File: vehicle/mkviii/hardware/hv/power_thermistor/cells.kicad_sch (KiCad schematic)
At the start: 53 parts, among them J10 Battery Cell Spot Weld, J11 Battery Cell Spot Weld, J12 Battery Cell Spot Weld, J13 Battery Cell Spot Weld, J14 Battery Cell Spot Weld, J15 Battery Cell Spot Weld, J16 Battery Cell Spot Weld, J17 Battery Cell Spot Weld, J18 Battery Cell Spot Weld, J19 Battery Cell Spot Weld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

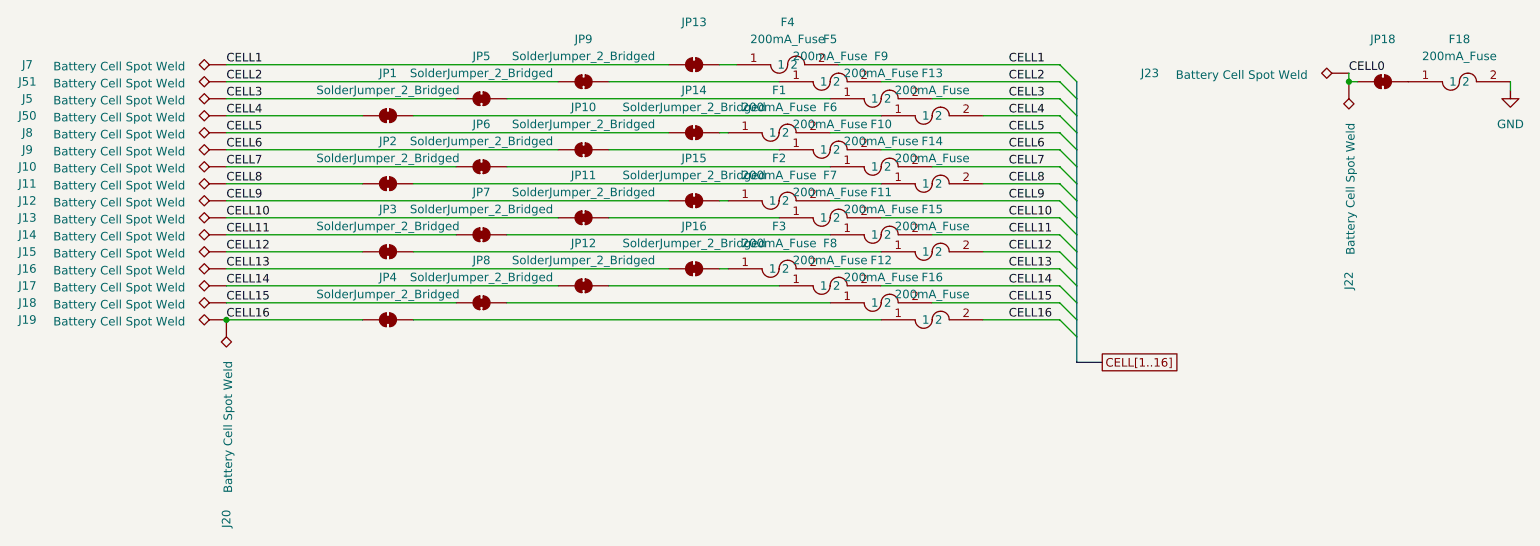
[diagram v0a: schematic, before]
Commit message: Minor redcube schematic changes; added some silkscreen; added production files
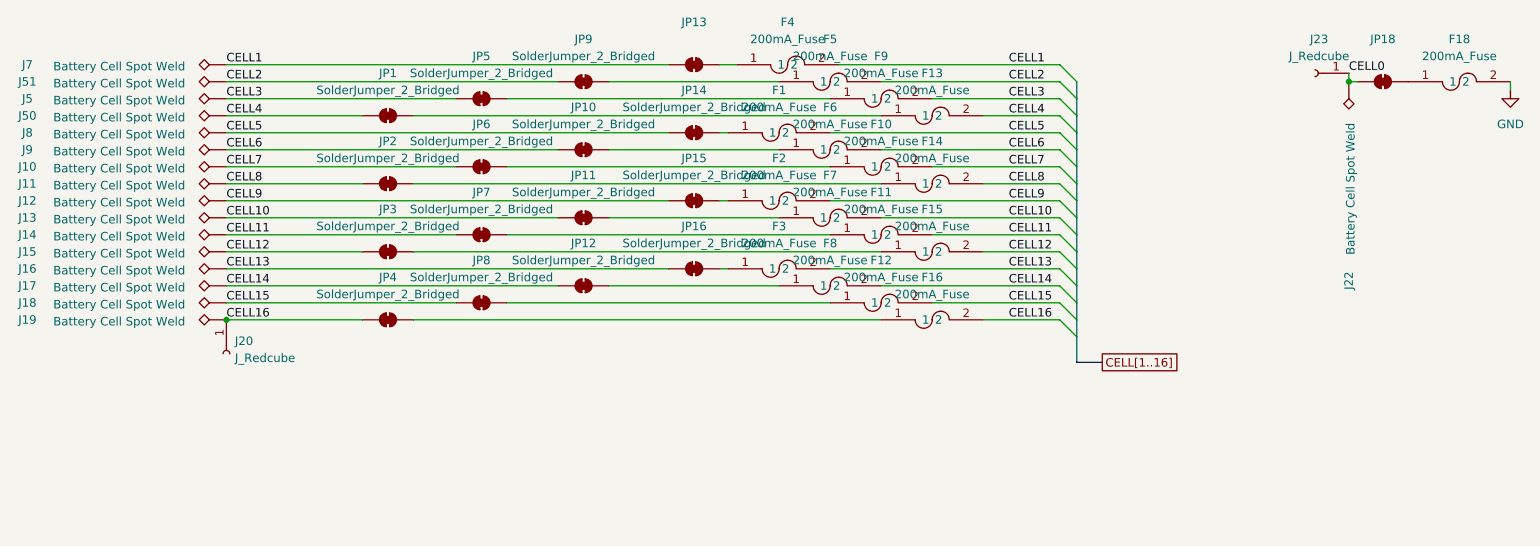
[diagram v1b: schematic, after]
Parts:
- removed J20, J23: Battery Cell Spot Weld, OEM:J_Bond_Pad_4p, symbol OEM:J_Battery_Cell_Spot_Weld
- added J20, J23: J_Redcube, OEM:Wurth-7461115, symbol OEM:J_Wurth_Redcube
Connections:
- net CELL0: now also J23.1 (Pin_1)
- net CELL16: now also J20.1 (Pin_1)
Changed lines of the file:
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@@
 	(title_block
 		(title "Power-Thermistor")
-		(date "2026-02-02")
-		(rev "2")
-		(comment 1 "Revised by Liam Fries")
+		(date "2026-04-15")
+		(rev "2.1")
+		(comment 1 "Revised by Liam Fries + Jacob Likins")
 		(comment 2 "Jake Hamilton")
 	)
@@
 	)
 	(symbol
+		(lib_id "OEM:J_Wurth_Redcube")
+		(at 236.22 33.02 180)
+		(unit 1)
+		(exclude_from_sim no)
+		(in_bom yes)
+		(on_board yes)
+		(dnp no)
+		(fields_autoplaced yes)
+		(property "Reference" "J23"
+			(at 236.855 27.94 0)
+			(effects
+				(font
+					(size 1.27 1.27)
+				)
+			)
+		)
+		(property "Value" "J_Redcube"
+			(at 236.855 30.48 0)
+			(effects
+				(font
+					(size 1.27 1.27)
+				)
+			)
+		)
+		(property "Footprint" "OEM:Wurth-7461115"
+			(at 236.22 33.02 0)
+			(effects
+				(font
+					(size 1.27 1.27)
+				)
+				(hide yes)
+			)
+		)
+		(property "Datasheet" "https://www.we-online.com/components/products/datasheet/7461115.pdf"
+			(at 236.22 33.02 0)
+			(effects
+				(font
+					(size 1.27 1.27)
+				)
+				(hide yes)
+			)
+		)
+		(property "Description" "TERM REDCUBE 25PIN PCB RA"
+			(at 236.22 33.02 0)
+			(effects
+				(font
+					(size 1.27 1.27)
+				)
+				(hide yes)
+			)
+		)
+		(property "MPN" "7461115"
+			(at 236.22 33.02 0)
+			(effects
+				(font
+					(size 1.27 1.27)
+				)
+				(hide yes)
+			)
+		)
+		(pin "1"
+		)
+		(instances
+			(project "power_thermistor"
+				(path "/9871410e-0b94-49cd-ba7d-079975b9e567/527cbe40-fc1c-43ac-87b7-ccac5898a8e8"
+					(reference "J23")
+					(unit 1)
+				)
+			)
+		)
+	)
+	(symbol
 		(lib_id "OEM:J_Battery_Cell_Spot_Weld")
 		(at 73.66 49.53 90)
@@
 	)
 	(symbol
-		(lib_id "OEM:J_Battery_Cell_Spot_Weld")
-		(at 73.66 69.85 180)
-		(unit 1)
-		(exclude_from_sim no)
-		(in_bom yes)
-		(on_board yes)
-		(dnp no)
-		(property "Reference" "J20"
-			(at 73.66 99.568 90)
-			(effects
-				(font
-					(size 1.27 1.27)
-				)
-			)
-		)
-		(property "Value" "Battery Cell Spot Weld"
-			(at 73.914 85.852 90)
-			(effects
-				(font
-					(size 1.27 1.27)
-				)
-			)
-		)
-		(property "Footprint" "OEM:J_Bond_Pad_4p"
-			(at 68.58 69.85 0)
-			(effects
-				(font
-					(size 1.27 1.27)
-				)
-				(hide yes)
-			)
-		)
-		(property "Datasheet" "~"
-			(at 68.58 69.85 0)
-			(effects
-				(font
-					(size 1.27 1.27)
-				)
-				(hide yes)
-			)
-		)
-		(property "Description" "Battery Cell Spot Weld"
-			(at 73.66 69.85 0)
-			(effects
-				(font
-					(size 1.27 1.27)
-				)
-				(hide yes)
-			)
-		)
-		(pin "1"
-		)
-		(instances
-			(project "power_thermistor"
-				(path "/9871410e-0b94-49cd-ba7d-079975b9e567/527cbe40-fc1c-43ac-87b7-ccac5898a8e8"
-					(reference "J20")
-					(unit 1)
-				)
-			)
-		)
-	)
-	(symbol
 		(lib_id "Jumper:SolderJumper_2_Bridged")
 		(at 111.76 57.15 0)
@@
 		(dnp no)
 		(fields_autoplaced yes)
-		(property "Reference" "#PWR?"
+		(property "Reference" "#PWR0133"
 			(at 265.43 41.91 0)
 			(effects
@@
 			(project "power_thermistor"
 				(path "/9871410e-0b94-49cd-ba7d-079975b9e567/527cbe40-fc1c-43ac-87b7-ccac5898a8e8"
-					(reference "#PWR?")
+					(reference "#PWR0133")
 					(unit 1)
 				)
@@
 	(symbol
 		(lib_id "OEM:J_Battery_Cell_Spot_Weld")
-		(at 241.3 33.02 90)
-		(unit 1)
-		(exclude_from_sim no)
-		(in_bom yes)
-		(on_board yes)
-		(dnp no)
-		(property "Reference" "J23"
-			(at 211.582 33.02 90)
-			(effects
-				(font
-					(size 1.27 1.27)
-				)
-			)
-		)
-		(property "Value" "Battery Cell Spot Weld"
-			(at 225.298 33.274 90)
-			(effects
-				(font
-					(size 1.27 1.27)
-				)
-			)
-		)
-		(property "Footprint" "OEM:J_Bond_Pad_4p"
-			(at 241.3 27.94 0)
-			(effects
-				(font
-					(size 1.27 1.27)
-				)
-				(hide yes)
-			)
-		)
-		(property "Datasheet" "~"
-			(at 241.3 27.94 0)
-			(effects
-				(font
-					(size 1.27 1.27)
-				)
-				(hide yes)
-			)
-		)
-		(property "Description" "Battery Cell Spot Weld"
-			(at 241.3 33.02 0)
-			(effects
-				(font
-					(size 1.27 1.27)
-				)
-				(hide yes)
-			)
-		)
-		(pin "1"
-		)
-		(instances
-			(project "power_thermistor"
-				(path "/9871410e-0b94-49cd-ba7d-079975b9e567/527cbe40-fc1c-43ac-87b7-ccac5898a8e8"
-					(reference "J23")
-					(unit 1)
-				)
-			)
-		)
-	)
-	(symbol
-		(lib_id "OEM:J_Battery_Cell_Spot_Weld")
 		(at 73.66 57.15 90)
 		(unit 1)
@@
 					(unit 1)
 				)
+			)
+		)
+	)
+	(symbol
+		(lib_id "OEM:J_Wurth_Redcube")
+		(at 73.66 74.93 270)
+		(unit 1)
+		(exclude_from_sim no)
+		(in_bom yes)
+		(on_board yes)
+		(dnp no)
+		(fields_autoplaced yes)
+		(property "Reference" "J20"
+			(at 74.93 73.0249 90)
+			(effects
+				(font
+					(size 1.27 1.27)
+				)
+				(justify left)
+			)
+		)
+		(property "Value" "J_Redcube"
+			(at 74.93 75.5649 90)
+			(effects
+				(font
+					(size 1.27 1.27)
+				)
+				(justify left)
+			)
+		)
+		(property "Footprint" "OEM:Wurth-7461115"
+			(at 73.66 74.93 0)
+			(effects
+				(font
+					(size 1.27 1.27)
+				)
+				(hide yes)
+			)
+		)
+		(property "Datasheet" "https://www.we-online.com/components/products/datasheet/7461115.pdf"
+			(at 73.66 74.93 0)
+			(effects
+				(font
+					(size 1.27 1.27)
+				)
+				(hide yes)
+			)
+		)
+		(property "Description" "TERM REDCUBE 25PIN PCB RA"
+			(at 73.66 74.93 0)
+			(effects
+				(font
+					(size 1.27 1.27)
+				)
+				(hide yes)
+			)
+		)
+		(property "MPN" "7461115"
+			(at 73.66 74.93 0)
+			(effects
+				(font
+					(size 1.27 1.27)
+				)
+				(hide yes)
+			)
+		)
+		(pin "1"
+		)
+		(instances
+			(project "power_thermistor"
+				(path "/9871410e-0b94-49cd-ba7d-079975b9e567/527cbe40-fc1c-43ac-87b7-ccac5898a8e8"
+					(reference "J20")
+					(unit 1)
+				)
